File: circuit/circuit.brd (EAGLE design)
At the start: 100 x 80 mm, 60 parts, among them IC1 74HC04N, X1 PSS 254/8G

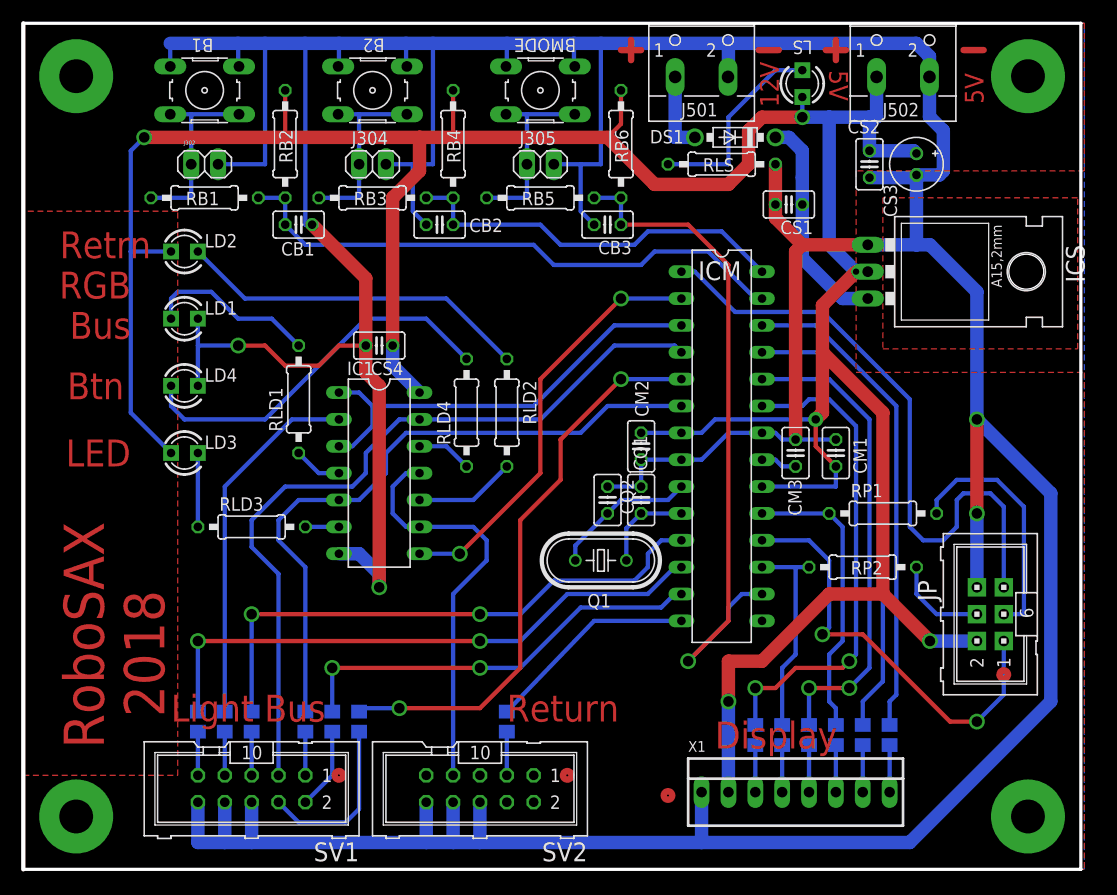
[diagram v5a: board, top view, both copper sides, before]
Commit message: updated layout of circuit board   + improved readability of labels   + added info labels to bottom   + added smiley
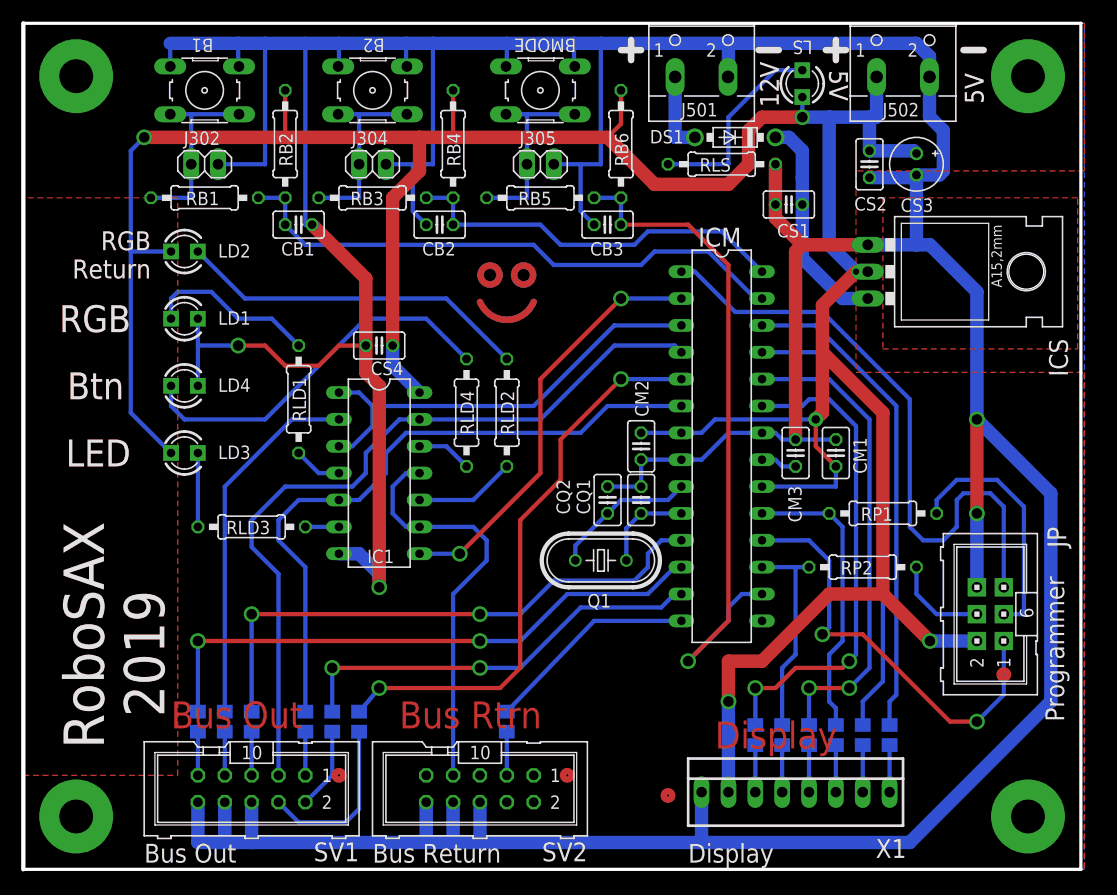
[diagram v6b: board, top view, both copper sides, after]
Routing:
- net N$40: track 0.00 -> 5.08 mm
- net N$36: track 0.00 -> 5.08 mm
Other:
- board text added: "29.04.2019"
- board text added: "Bus Out"
- board text added: "Bus Return"
- board text added: "Bus Rtrn"
- board text added: "Peter Weissig"
- board text added: "Programmer"
- board text added: "RGB Return"
- board text added: "RoboSAX 2019"
- board text added: "https://github.com/RoboSAX/eagle_spielfeld"
- board text removed: "Bus"
- board text removed: "Light Bus"
- board text removed: "Retrn"
- board text removed: "Return"
- board text removed: "RoboSAX 2018"

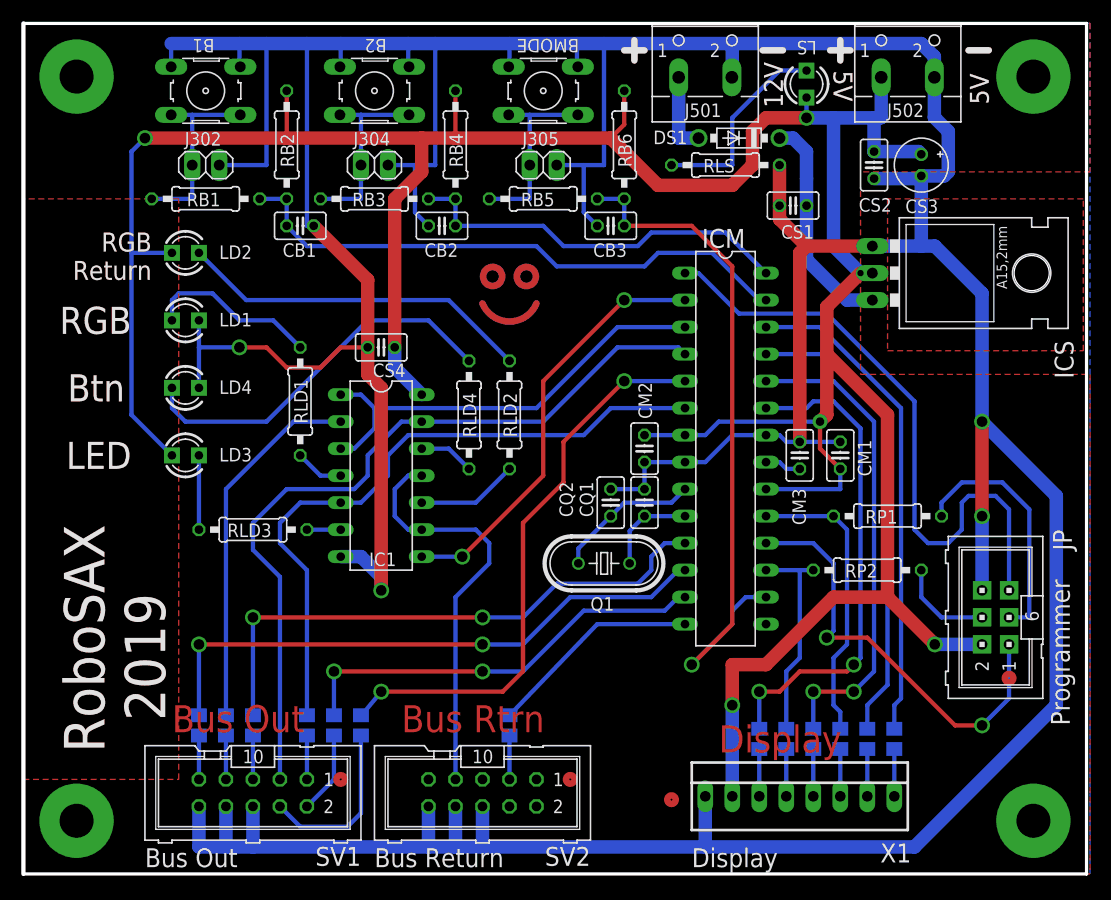
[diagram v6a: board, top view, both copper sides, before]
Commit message: updated circuit   + changed font type and size (e.g. fixed size of url)   + updated cooling pad for voltage regulator   + added more spacing at buttons (between pinheads and resistors)   + updated part-list
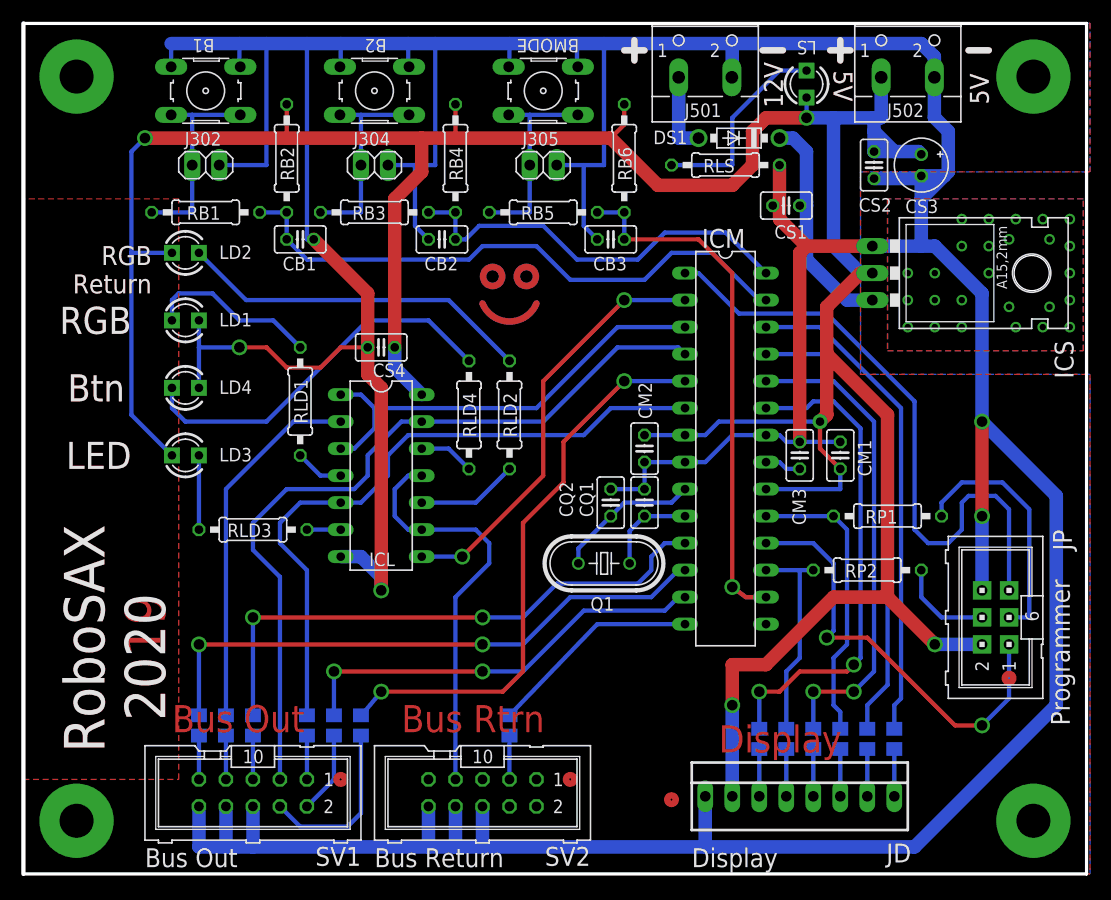
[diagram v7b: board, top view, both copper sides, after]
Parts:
- moved CB1 1.27 mm to (26.0, 59.7)
- moved CB2 1.27 mm to (39.4, 59.7)
- moved CB3 1.27 mm to (55.2, 59.7)
- moved RB1 1.27 mm to (17.1, 62.2)
- moved RB3 1.27 mm to (33.0, 62.2)
- moved RB5 1.27 mm to (48.9, 62.2)
- moved RB2 1.27 mm to (24.8, 67.3)
- moved RB4 1.27 mm to (40.6, 67.3)
- moved RB6 1.27 mm to (56.5, 67.3)
- moved CS1 0.64 mm to (71.8, 62.9)
- renumbered IC1 to ICL, X1 to JD
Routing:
- net BTN3: track 66.2 -> 53.1 mm
- net GND: track 501.2 -> 507.4 mm
- net BTN2: track 37.2 -> 38.8 mm
- net BTN1: track 54.1 -> 55.7 mm
- net N$6: track 18.2 -> 19.5 mm
- net N$4: track 18.2 -> 19.5 mm
- net N$10: track 18.2 -> 19.5 mm
- net N$5: track 21.0 -> 21.6 mm
- net +5V: vias 6 -> 5
- added copper zone on layer 16, net ICS_TAB
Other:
- board text added: "06.11.2019"
- board text added: "RoboSAX 2020"
- board text added: "github.com/RoboSAX/eagle_spielfeld"
- board text removed: "29.04.2019"
- board text removed: "https://github.com/RoboSAX/eagle_spielfeld"

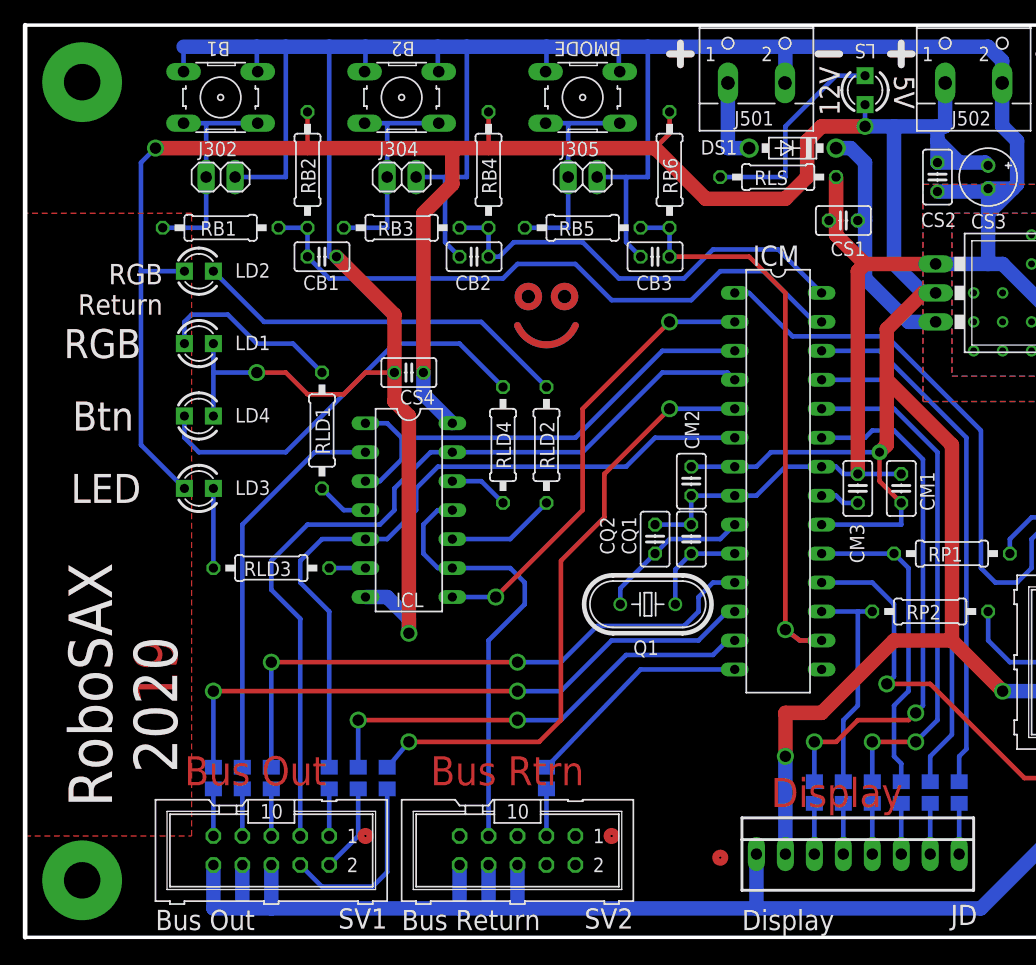
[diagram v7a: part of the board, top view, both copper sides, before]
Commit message: minor fixes:   + updated crystal from 16 to 20 MHz   + updated package for SMD resistors (1206 instead of 0805)   + fixed wrong caption (from 2019 to 2020) ==> newly exported images and elecrow files ==> updated part list and reichelt shopping cart
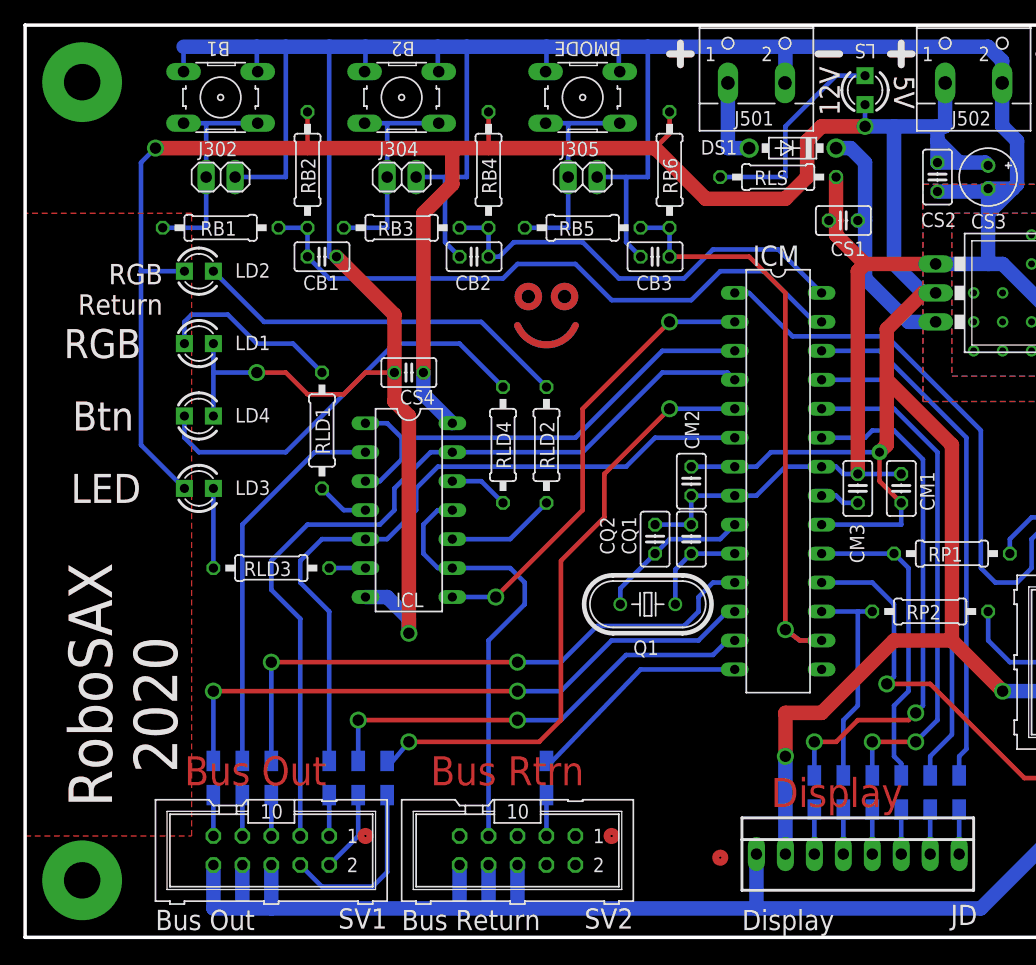
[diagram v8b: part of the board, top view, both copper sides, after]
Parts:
- R1, R10, R11, R12, R13, R2, R3, R4, R5, R6, R7, R8, R9: device rcl:R0805 -> rcl:R1206W
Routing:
- net N$19: track 7.72 -> 7.17 mm
- net N$18: track 16.2 -> 15.7 mm
- net N$1: track 4.13 -> 3.58 mm
- net BUS_LED_LOAD: track 40.0 -> 39.5 mm
- net BUS_LED_DATA: track 62.8 -> 62.3 mm
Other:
- board text added: "17.11.2019"
- board text added: "20MHz"
- board text removed: "06.11.2019"
- board text removed: "RoboSAX 2019"
